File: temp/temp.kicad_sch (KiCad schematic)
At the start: 1 part

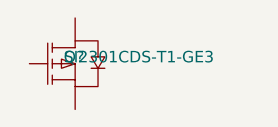
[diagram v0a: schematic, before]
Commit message: Changed switch
Changed switch do not depend on p-mosfet
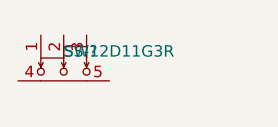
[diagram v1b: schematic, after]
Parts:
- removed Q?: SI2301CDS-T1-GE3, SOT-23-3_L3.0-W1.7-P0.95-LS2.9-BR, symbol temp-altium-import:root_0_SI2301CDS-T1-GE3_
- added SW?: SS-12D11G3R, SW-TH_SS-12D11L3, symbol temp-altium-import:root_0_SS-12D11G3R_
